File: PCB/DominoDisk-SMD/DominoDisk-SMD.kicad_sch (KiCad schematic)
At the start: 28 parts, among them J1 Daisy port out, J2 ICSP_ISP6, J3 UART, J4 Daisy port in, K1 HYC77-TF09-200, U1 PC817C-S, U2 ATmega328P-AU, U3 SE5218, U4 TXB0104QPWRQ1, Y1 Crystal_GND2

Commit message: Same on Domino
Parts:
- C2: value 100nF -> 100n; LCSC C28233 -> C1590
- R4: value 10K -> 10k; LCSC C17414 -> C177337
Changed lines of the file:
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@@
 			)
 		)
-		(property "Value" "100nF"
+		(property "Value" "100n"
 			(at 25.7048 118.11 90)
 			(effects
@@
 			)
 		)
-		(property "LCSC" "C28233"
+		(property "LCSC" " C1590"
 			(at 29.21 118.11 90)
 			(effects
@@
 			)
 		)
-		(property "Value" "10K"
+		(property "Value" "10k"
 			(at 108.4072 147.193 0)
 			(effects
@@
 			)
 		)
-		(property "LCSC" "C17414"
+		(property "LCSC" " C177337"
 			(at 106.68 146.05 0)
 			(effects

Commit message: Add libraries and update Domino/Angled
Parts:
- K1: footprint MICROSD-HYC77-TF09-200:MICROSD-HYC77-TF09-200 -> HYC04-TF09-200:MICROSD-HYC77-TF09-200
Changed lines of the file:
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@@
 			)
 		)
-		(property "Footprint" "MICROSD-HYC77-TF09-200:MICROSD-HYC77-TF09-200"
+		(property "Footprint" "HYC04-TF09-200:MICROSD-HYC77-TF09-200"
 			(at 269.24 50.8 0)
 			(effects

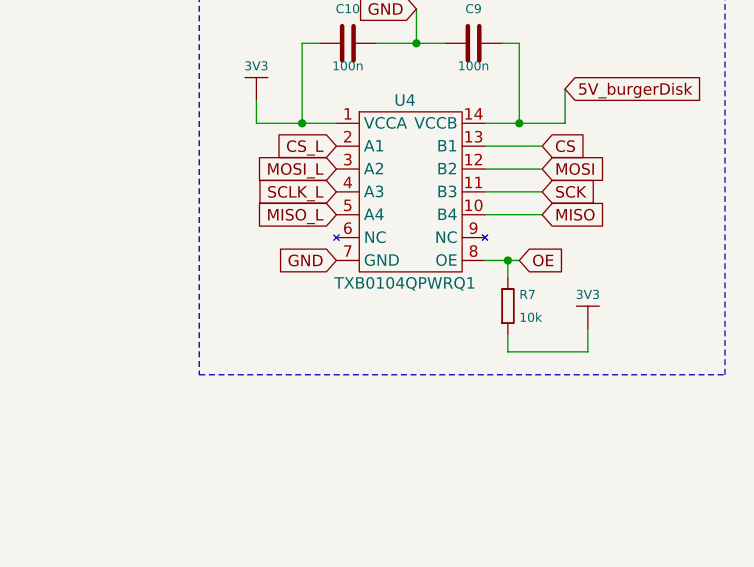
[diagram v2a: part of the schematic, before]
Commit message: Add logo (thanks to Javier Rivera!!)
Add my own micro/SD modules
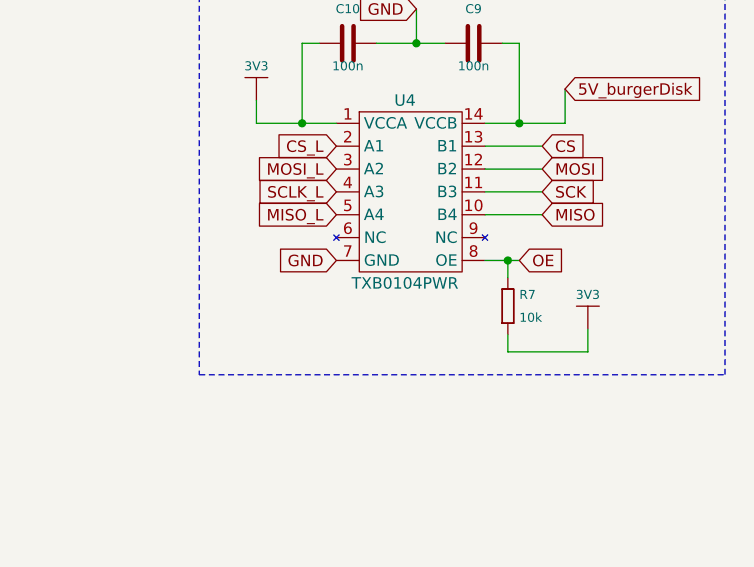
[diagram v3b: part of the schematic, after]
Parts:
- U4: value TXB0104QPWRQ1 -> TXB0104PWR; LCSC C527571 -> C60708
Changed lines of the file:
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@@
 			)
 		)
-		(property "Value" "TXB0104QPWRQ1"
+		(property "Value" "TXB0104PWR"
 			(at 245.11 149.86 0)
 			(effects
@@
 			)
 		)
-		(property "LCSC" "C527571"
+		(property "LCSC" "C60708"
 			(at 245.11 138.43 0)
 			(effects

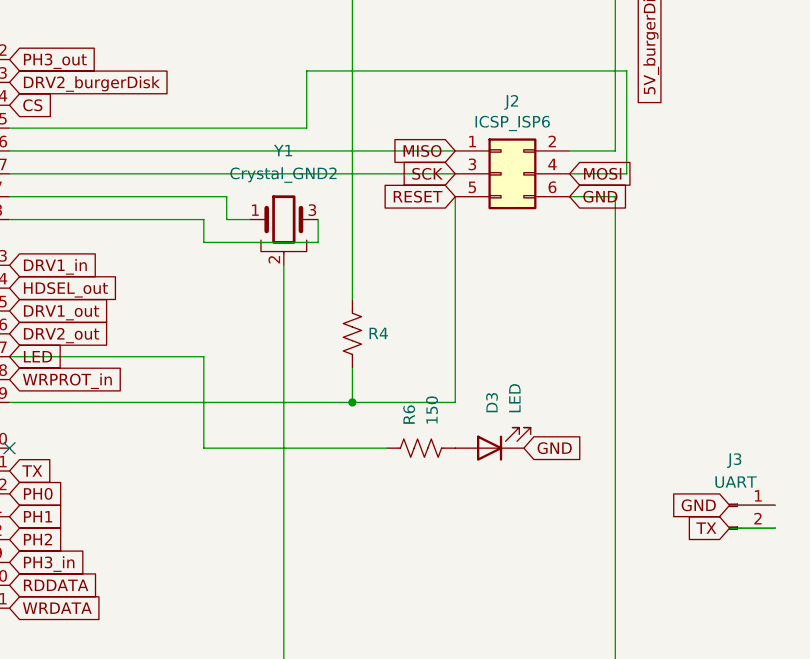
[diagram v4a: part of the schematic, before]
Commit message: Fix LED and R6
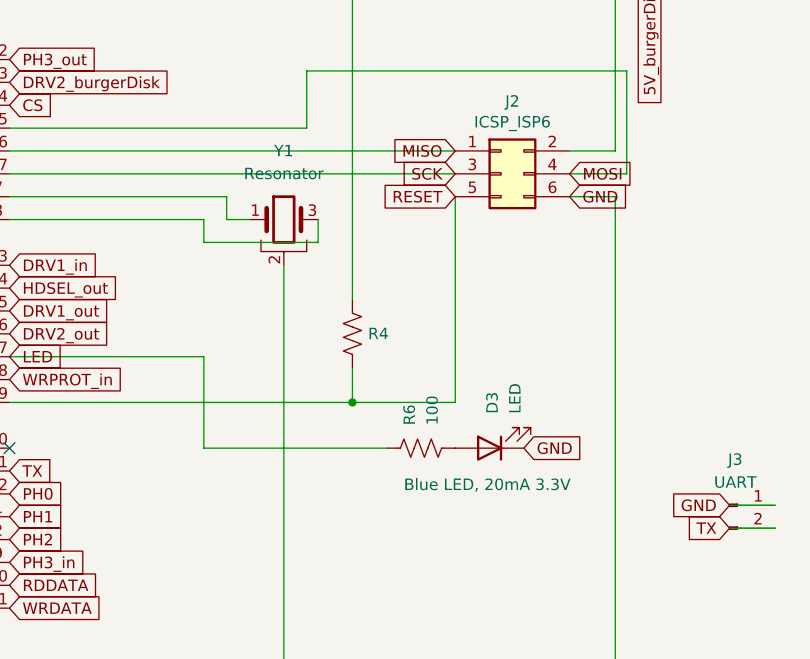
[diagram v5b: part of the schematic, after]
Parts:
- D3: LCSC C2288 -> C965807
- R6: value 150 -> 100; LCSC C177290 -> C22369795
- Y1: value Crystal_GND2 -> Resonator
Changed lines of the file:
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@@
 		(on_board yes)
 		(dnp no)
-		(fields_autoplaced yes)
 		(property "Reference" "D3"
 			(at 122.2375 154.94 90)
@@
 			)
 		)
-		(property "Description" ""
-			(at 121.92 158.75 0)
-			(effects
-				(font
-					(size 1.27 1.27)
-				)
-			)
-		)
-		(property "LCSC" "C2288"
+		(property "Description" "Blue LED, 20mA 3.3V"
+			(at 121.666 162.814 0)
+			(effects
+				(font
+					(size 1.27 1.27)
+				)
+			)
+		)
+		(property "LCSC" "C965807"
 			(at 121.92 158.75 0)
 			(effects
@@
 			)
 		)
-		(property "Value" "150"
+		(property "Value" "100"
 			(at 115.57 156.21 0)
 			(effects
@@
 			)
 		)
-		(property "LCSC" "C177290"
+		(property "LCSC" "C22369795"
 			(at 114.3 158.75 0)
 			(effects
@@
 			)
 		)
-		(property "Value" "Crystal_GND2"
+		(property "Value" "Resonator"
 			(at 99.06 128.27 0)
 			(effects
@@
 			)
 		)
-		(property "Description" "Three pin crystal, GND on pin 2"
+		(property "Description" "Three pin, GND on pin 2"
 			(at 99.06 133.35 0)
 			(effects

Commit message: More OCD
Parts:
- renumbered C5 to C1, C6 to C2, C7 to C3, C8 to C4, C4 to C5, C9 to C6, C10 to C7, C2 to C8, D3 to D1, D1 to D2, D2 to D3, J4 to J3, J3 to J4, R6 to R1, R4 to R2, R1 to R3, R3 to R4, R2 to R6, U3 to U2, U2 to U3
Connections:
- net GND: now also K1.SHIELD
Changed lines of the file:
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@@
 		)
 	)
+	(global_label "GND"
+		(shape input)
+		(at 275.59 26.67 270)
+		(fields_autoplaced yes)
+		(effects
+			(font
+				(size 1.27 1.27)
+			)
+			(justify right)
+		)
+		(property "Intersheetrefs" "${INTERSHEET_REFS}"
+			(at 275.59 33.5257 90)
+			(effects
+				(font
+					(size 1.27 1.27)
+				)
+				(justify right)
+				(hide yes)
+			)
+		)
+	)
 	(global_label "PH0"
 		(shape input)
@@
 		(on_board yes)
 		(dnp no)
-		(property "Reference" "C10"
+		(property "Reference" "C7"
 			(at 238.76 119.38 0)
 			(effects
@@
 			(project "Small"
 				(path "/596d0583-1d97-453e-b84c-75eed809afa2"
-					(reference "C10")
+					(reference "C7")
 					(unit 1)
 				)
@@
 		(on_board yes)
 		(dnp no)
-		(property "Reference" "C2"
+		(property "Reference" "C8"
 			(at 25.4 118.11 90)
 			(effects
@@
 			(project "Small-atmega-SMD"
 				(path "/596d0583-1d97-453e-b84c-75eed809afa2"
-					(reference "C2")
+					(reference "C8")
 					(unit 1)
 				)
@@
 		(on_board yes)
 		(dnp no)
-		(property "Reference" "J3"
+		(property "Reference" "J4"
 			(at 149.225 160.02 0)
 			(effects
@@
 			(project "BurgerDisk_THT_AngledDB19"
 				(path "/596d0583-1d97-453e-b84c-75eed809afa2"
-					(reference "J3")
+					(reference "J4")
 					(unit 1)
 				)
@@
 		(on_board yes)
 		(dnp no)
-		(property "Reference" "D2"
+		(property "Reference" "D3"
 			(at 53.34 76.2 90)
 			(effects
@@
 			(project "BurgerDisk_THT_AngledDB19"
 				(path "/596d0583-1d97-453e-b84c-75eed809afa2"
-					(reference "D2")
+					(reference "D3")
 					(unit 1)
 				)
@@
 		(on_board yes)
 		(dnp no)
-		(property "Reference" "U2"
+		(property "Reference" "U3"
 			(at 53.34 189.23 0)
 			(effects
@@
 			(project "Small-atmega-SMD"
 				(path "/596d0583-1d97-453e-b84c-75eed809afa2"
-					(reference "U2")
+					(reference "U3")
 					(unit 1)
 				)
@@
 		(on_board yes)
 		(dnp no)
-		(property "Reference" "U3"
+		(property "Reference" "U2"
 			(at 251.46 83.185 0)
 			(effects
@@
 			(project "Small"
 				(path "/596d0583-1d97-453e-b84c-75eed809afa2"
-					(reference "U3")
+					(reference "U2")
 					(unit 1)
 				)
@@
 		(on_board yes)
 		(dnp no)
-		(property "Reference" "R2"
+		(property "Reference" "R6"
 			(at 102.87 83.82 0)
 			(effects
@@
 			(project "BurgerDisk_THT_AngledDB19"
 				(path "/596d0583-1d97-453e-b84c-75eed809afa2"
-					(reference "R2")
+					(reference "R6")
 					(unit 1)
 				)
@@
 		(on_board yes)
 		(dnp no)
-		(property "Reference" "C5"
+		(property "Reference" "C1"
 			(at 229.87 35.56 90)
 			(effects
@@
 			(project "Small"
 				(path "/596d0583-1d97-453e-b84c-75eed809afa2"
-					(reference "C5")
+					(reference "C1")
 					(unit 1)
 				)
@@
 		(on_board yes)
 		(dnp no)
-		(property "Reference" "C4"
+		(property "Reference" "C5"
 			(at 269.24 86.995 90)
 			(effects
@@
 			(project "Small"
 				(path "/596d0583-1d97-453e-b84c-75eed809afa2"
-					(reference "C4")
+					(reference "C5")
 					(unit 1)
 				)
@@
 		(pin "8"
 		)
+		(pin "SHIELD"
+		)
 		(instances
 			(project "Small"
@@
 		(on_board yes)
 		(dnp no)
-		(property "Reference" "R4"
+		(property "Reference" "R2"
 			(at 108.4072 146.05 0)
 			(effects
@@
 			(project "Small-atmega-SMD"
 				(path "/596d0583-1d97-453e-b84c-75eed809afa2"
-					(reference "R4")
+					(reference "R2")
 					(unit 1)
 				)
@@
 		(dnp no)
 		(fields_autoplaced yes)
-		(property "Reference" "R1"
+		(property "Reference" "R3"
 			(at 74.93 66.04 0)
 			(effects
@@
 			(project "BurgerDisk_THT_AngledDB19"
 				(path "/596d0583-1d97-453e-b84c-75eed809afa2"
-					(reference "R1")
+					(reference "R3")
 					(unit 1)
 				)
@@
 		(on_board yes)
 		(dnp no)
-		(property "Reference" "D3"
+		(property "Reference" "D1"
 			(at 122.2375 154.94 90)
 			(effects
@@
 			(project "Small-atmega-SMD"
 				(path "/596d0583-1d97-453e-b84c-75eed809afa2"
-					(reference "D3")
+					(reference "D1")
 					(unit 1)
 				)
@@
 		(on_board yes)
 		(dnp no)
-		(property "Reference" "C6"
+		(property "Reference" "C2"
 			(at 237.49 35.56 90)
 			(effects
@@
 			(project "Small"
 				(path "/596d0583-1d97-453e-b84c-75eed809afa2"
-					(reference "C6")
+					(reference "C2")
 					(unit 1)
 				)
@@
 		(on_board yes)
 		(dnp no)
-		(property "Reference" "C7"
+		(property "Reference" "C3"
 			(at 245.11 35.56 90)
 			(effects
@@
 			(project "Small"
 				(path "/596d0583-1d97-453e-b84c-75eed809afa2"
-					(reference "C7")
+					(reference "C3")
 					(unit 1)
 				)
@@
 		(dnp no)
 		(fields_autoplaced yes)
-		(property "Reference" "R6"
+		(property "Reference" "R1"
 			(at 113.03 156.21 0)
 			(effects
@@
 			(project "Small-atmega-SMD"
 				(path "/596d0583-1d97-453e-b84c-75eed809afa2"
-					(reference "R6")
+					(reference "R1")
 					(unit 1)
 				)
@@
 		(on_board yes)
 		(dnp no)
-		(property "Reference" "C8"
+		(property "Reference" "C4"
 			(at 238.76 88.265 90)
 			(effects
@@
 			(project "Small"
 				(path "/596d0583-1d97-453e-b84c-75eed809afa2"
-					(reference "C8")
+					(reference "C4")
 					(unit 1)
 				)
@@
 		(dnp no)
 		(fields_autoplaced yes)
-		(property "Reference" "D1"
+		(property "Reference" "D2"
 			(at 143.1925 99.06 0)
 			(effects
@@
 			(project "Small-atmega-SMD"
 				(path "/596d0583-1d97-453e-b84c-75eed809afa2"
-					(reference "D1")
+					(reference "D2")
 					(unit 1)
 				)
@@
 		(on_board yes)
 		(dnp no)
-		(property "Reference" "C9"
+		(property "Reference" "C6"
 			(at 252.73 119.38 0)
 			(effects
@@
 			(project "Small"
 				(path "/596d0583-1d97-453e-b84c-75eed809afa2"
-					(reference "C9")
+					(reference "C6")
 					(unit 1)
 				)
@@
 		(dnp no)
 		(fields_autoplaced yes)
-		(property "Reference" "R3"
+		(property "Reference" "R4"
 			(at 100.33 68.58 0)
 			(effects
@@
 			(project "BurgerDisk_THT_AngledDB19"
 				(path "/596d0583-1d97-453e-b84c-75eed809afa2"
-					(reference "R3")
+					(reference "R4")
 					(unit 1)
 				)
@@
 		(dnp no)
 		(fields_autoplaced yes)
-		(property "Reference" "J4"
+		(property "Reference" "J3"
 			(at 34.29 20.32 0)
 			(effects
@@
 			(project ""
 				(path "/596d0583-1d97-453e-b84c-75eed809afa2"
-					(reference "J4")
+					(reference "J3")
 					(unit 1)
 				)

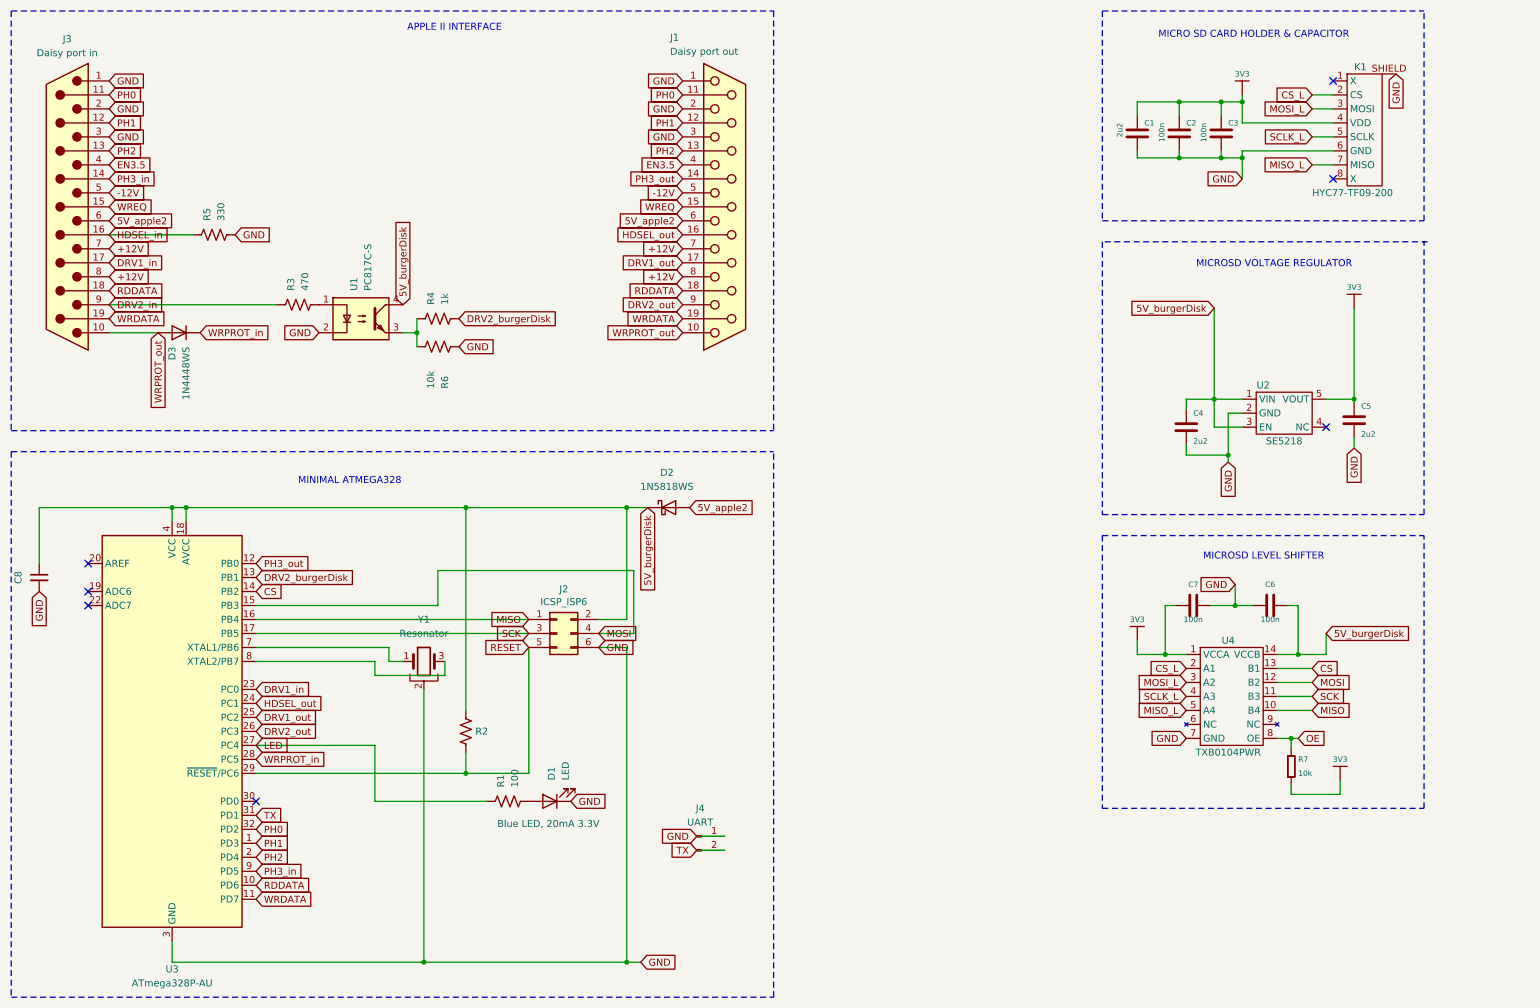
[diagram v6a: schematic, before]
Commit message: Enable teardrops
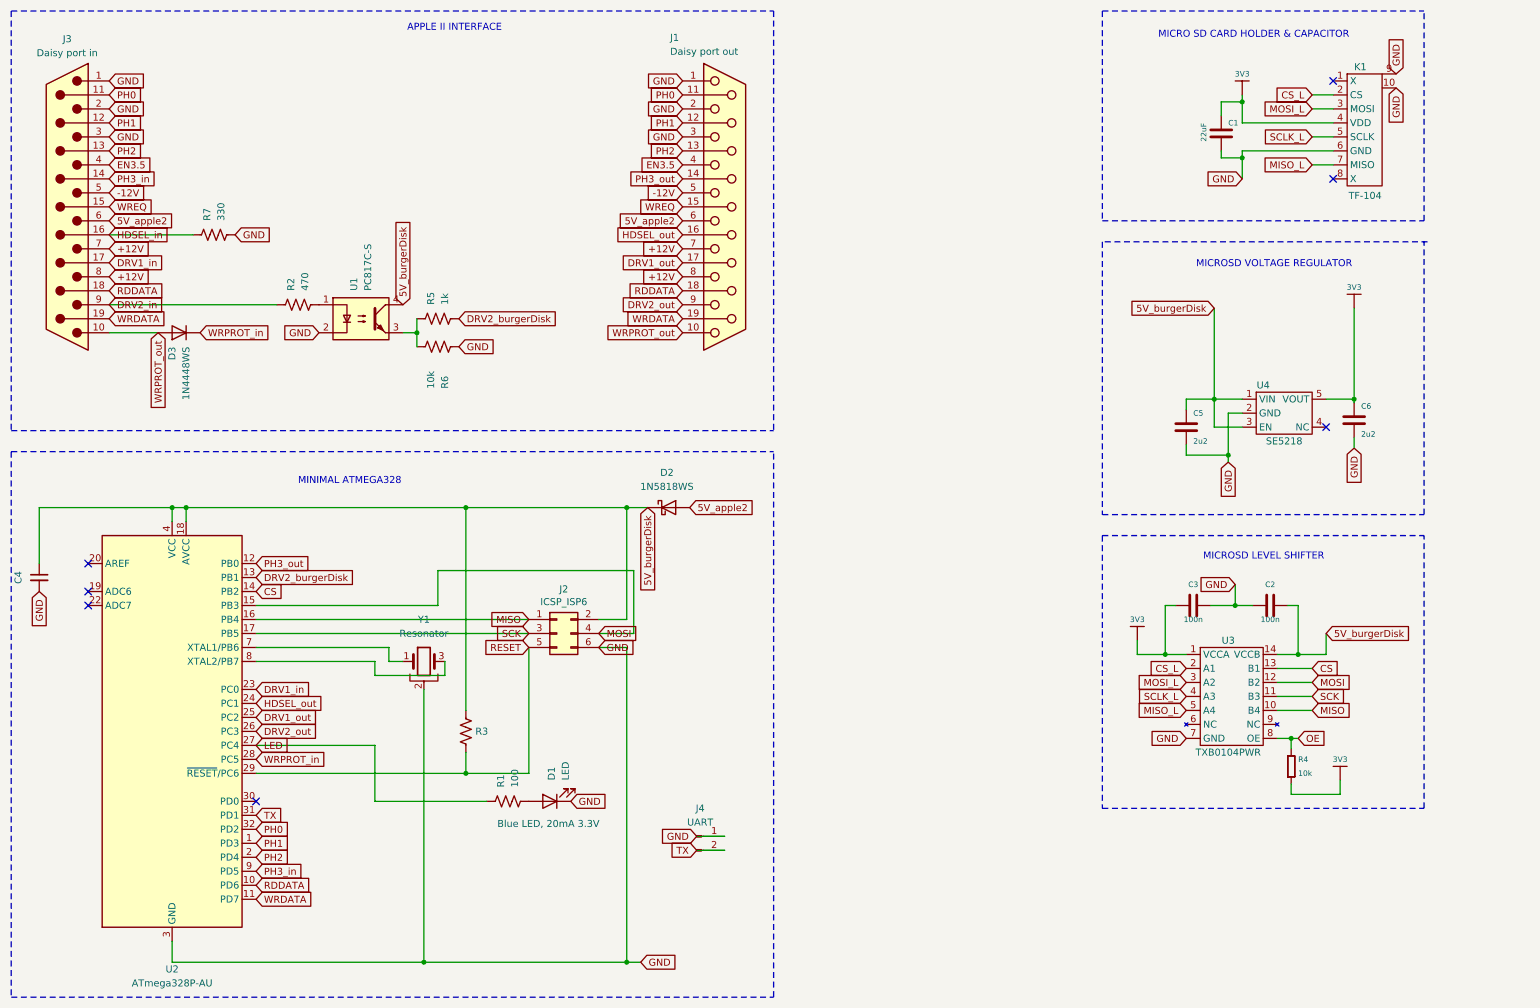
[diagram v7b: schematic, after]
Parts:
- removed C1: 2u2, Capacitor_SMD:C_0603_1608Metric, symbol e-radionica.com schematics:0603C
- removed C2: 100n, Capacitor_SMD:C_0603_1608Metric, symbol e-radionica.com schematics:0603C
- C1: renamed from C3; value 100n -> 22uF; footprint Capacitor_SMD:C_0603_1608Metric -> Capacitor_SMD:C_0805_2012Metric; LCSC C1590 -> C45783
- J4: footprint Connector_PinHeader_2.54mm:PinHeader_1x02_P2.54mm_Horizontal -> Connector_PinHeader_2.54mm:PinHeader_1x02_P2.54mm_Vertical
- K1: value HYC77-TF09-200 -> TF-104; footprint HYC04-TF09-200:MICROSD-HYC77-TF09-200 -> TF-104:TF-SMD_TF-104; LCSC C341092 -> C266612
- renumbered C6 to C2, C7 to C3, C8 to C4, C4 to C5, C5 to C6, R3 to R2, R2 to R3, R7 to R4, R4 to R5, R5 to R7, U3 to U2, U4 to U3, U2 to U4
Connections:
- net GND: now also K1.10, K1.9; no longer K1.SHIELD

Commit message: micro changes
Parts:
- K1: value TF-104 -> TF-104 MicroSD card holder
- U3: value TXB0104PWR -> TXB0104PWR level shifter
- U4: value SE5218 -> SE5218 voltage regulator
- Y1: value Resonator -> CSTNE16M0V530000R0 Resonator
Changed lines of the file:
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@@
 			)
 		)
-		(property "Description" ""
-			(at 148.59 165.1 0)
+		(property "Description" "Debug header - do not assemble"
+			(at 149.352 170.688 0)
 			(effects
 				(font
@@
 			)
 		)
-		(property "Value" "SE5218"
+		(property "Value" "SE5218 voltage regulator"
 			(at 255.27 93.345 0)
 			(effects
@@
 			)
 		)
-		(property "Value" "TF-104"
+		(property "Value" "TF-104 MicroSD card holder"
 			(at 266.954 48.768 0)
 			(effects
@@
 			)
 		)
-		(property "Description" ""
-			(at 123.19 128.27 0)
+		(property "Description" "2x3 pins male header, 2.54mm pitch, horizontal"
+			(at 133.096 134.112 0)
 			(effects
 				(font
@@
 			)
 		)
-		(property "Value" "TXB0104PWR"
+		(property "Value" "TXB0104PWR level shifter"
 			(at 245.11 149.86 0)
 			(effects
@@
 			)
 		)
-		(property "Value" "Resonator"
+		(property "Value" "CSTNE16M0V530000R0 Resonator"
 			(at 99.06 128.27 0)
 			(effects
